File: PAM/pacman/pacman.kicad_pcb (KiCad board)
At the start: 2 copper layers, 92.7 x 66 mm, 20 parts, among them J1 Conn_01x08, J2 Conn_01x04, J6 TE Mate-N-Lok, J7 TE Mate-N-Lok, J8 TE Mate-N-Lok, J9 JST PH, K1 G2RL, K2 G5V-1, Q2 MMBT2222A

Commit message: working on layout
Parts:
- moved J7 77.4 mm to (72.9, 96.0), turned to 180 degrees
- moved R7 52.2 mm to (57.4, 124.2), turned to 90 degrees
- moved R4 51.0 mm to (47.5, 124.5), turned to 90 degrees
- moved F2 41.6 mm to (73.2, 119.4), turned to 90 degrees
- moved J8 38.1 mm to (86.7, 97.3)
- moved K1 31.5 mm to (40.3, 133.6)
- moved D1 30.8 mm to (87.6, 86.4), turned to 90 degrees
- moved D3 30.7 mm to (32.8, 133.3)
- moved R1 29.0 mm to (60.7, 79.0)
- moved F1 17.2 mm to (85.9, 125.2), turned to 90 degrees
- moved Q2 7.95 mm to (31.6, 112.8)
- moved R6 7.75 mm to (29.9, 107.2)
- moved R5 7.63 mm to (29.9, 109.2)
- moved J6 4.57 mm to (46.5, 80.4), turned to 90 degrees
- moved D5 0.76 mm to (14.7, 108.0), turned to -90 degrees
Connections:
- D3 pad 1: /TSV_SAFETY_LOOP -> /AIR_B-
- D5 pad 1: /TSV_SAFETY_LOOP -> /AIR_B-
- J1 pad 1: +12V -> GND
- J1 pad 2: /PRECHARGE -> GND
- J1 pad 3: /TSV_SAFETY_LOOP -> +12V
- J1 pad 4: /BMS_CAN+ -> /PRECHARGE
- J1 pad 5: /BMS_CAN- -> /BMS_CAN+
- J1 pad 6: /MAIN_CONT -> /AIR_B-
- J1 pad 7: unconnected-(J1-Pad7) -> /MAIN_CONT
- J1 pad 8: GND -> /BMS_CAN-
- J9 pad 1: /TSV_SAFETY_LOOP -> /AIR_B-
- K1 pad 2: /TSV_SAFETY_LOOP -> /AIR_B-
- K2 pad 10: /TSV_SAFETY_LOOP -> /AIR_B-
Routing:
- net /AIR_B-: track 0.00 -> 33.4 mm
- net /BMS_CAN+: track 0.00 -> 31.7 mm
- net /BMS_CAN-: track 0.00 -> 31.7 mm
- net +12V: track 0.00 -> 31.5 mm
- net /AIR_B+: track 0.00 -> 27.4 mm
- net /MAIN_CONT: track 0.00 -> 26.0 mm
- net /PRECHARGE: track 0.00 -> 22.3 mm
- net Net-(Q2-Pad1): track 0.00 -> 2.65 mm
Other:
- outline, holes or cut-outs redrawn

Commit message: DRC updating
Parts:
- removed J7, J8: TE Mate-N-Lok, AERO_Footprints:TE_MATE-N-LOK_1-770866-x_1x02_P4.14mm_Vertical
- added F3: Fuse, AERO_Footprints:Fuseholder_Blade_Mini_Keystone_3568, F.Cu at (185.0, 64.1)
- added G***: LOGO, AERO_Footprints:AERO_Logo_10x4mm, F.Cu at (181.1, 109.2)
- added High Voltage: Symbol_HighVoltage_Type2_CopperTop_VerySmall, Symbol:Symbol_HighVoltage_Type2_CopperTop_VerySmall, F.Cu at (129.8, 109.0)
- added J3: Conn_01x01, Connector_Hirose:Hirose_DF63M-1P-3.96DSA_1x01_P3.96mm_Vertical, F.Cu at (155.7, 111.0)
- added J4: Conn_01x01, Connector_Hirose:Hirose_DF63M-1P-3.96DSA_1x01_P3.96mm_Vertical, F.Cu at (129.3, 93.5)
- added J5: Conn_01x01, Connector_Hirose:Hirose_DF63M-1P-3.96DSA_1x01_P3.96mm_Vertical, F.Cu at (117.3, 106.9)
- added K3: G5V-1, Relay_THT:Relay_SPDT_Omron_G5V-1, F.Cu at (198.7, 63.4)
- D1: footprint LED_SMD:LED_0603_1608Metric_Pad1.05x0.95mm_HandSolder -> AERO_Footprints:LPA-C011301S-x LED 0805 LIGHT PIPE SINGLE VERT SMD
- D3, R1: moved to B.Cu
- J6: value TE Mate-N-Lok -> Conn_01x02; footprint AERO_Footprints:TE_MATE-N-LOK_1-770866-x_1x02_P4.14mm_Vertical -> Connector_JST:JST_XH_B2B-XH-A_1x02_P2.50mm_Vertical
- moved J2 193.6 mm to (195.6, 78.7), turned to 90 degrees
- moved J9 177.0 mm to (188.0, 78.0), turned to 90 degrees
- moved D5 174.8 mm to (187.8, 83.7), turned to 90 degrees
- moved K2 163.8 mm to (181.6, 79.9), turned to 180 degrees
- moved J1 163.3 mm to (182.9, 98.9), turned to 0 degrees
- moved D4 162.4 mm to (179.2, 73.0), turned to 180 degrees
- moved D3 156.4 mm to (172.1, 62.4), turned to 90 degrees
- moved R5 145.2 mm to (172.7, 82.4), turned to 0 degrees
- moved R6 144.5 mm to (172.7, 84.5), turned to 0 degrees
- moved Q2 143.5 mm to (171.0, 78.9), turned to 180 degrees
- moved K1 135.0 mm to (154.9, 62.4), turned to 180 degrees
- moved J6 133.7 mm to (178.1, 56.4), turned to -90 degrees
- moved R4 119.2 mm to (155.1, 73.0), turned to -90 degrees
- moved R7 101.5 mm to (145.2, 73.3), turned to -90 degrees
- moved R1 86.7 mm to (140.7, 112.3), turned to 90 degrees
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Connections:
- J1 pad 2: GND -> /BMS_FAN
- J6 pad 1: /INT+ -> Net-(F3-Pad2)
- J6 pad 2: /INT+ -> GND
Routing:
- net /INT-: track 0.00 -> 52.0 mm
- net /BMS_FAN: track 0.00 -> 47.7 mm
- net Net-(F1-Pad1): track 0.00 -> 40.8 mm
- net +12V: track 31.5 -> 70.3 mm
- net /INT+: track 0.00 -> 28.5 mm
- net Net-(D3-Pad2): track 0.00 -> 24.3 mm, vias 0 -> 1
- net /AIR_B-: track 33.4 -> 56.2 mm
- net Net-(K1-Pad5): track 0.00 -> 18.3 mm
- net Net-(F2-Pad1): track 0.00 -> 14.6 mm
- net Net-(D1-Pad2): track 0.00 -> 13.0 mm
- net Net-(F3-Pad2): track 0.00 -> 11.2 mm
- net /FAN_OUT: track 0.00 -> 8.82 mm
- net /B+: track 0.00 -> 7.26 mm
- net /BMS_CAN+: track 31.7 -> 28.7 mm
- net /BMS_CAN-: track 31.7 -> 28.7 mm
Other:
- outline, holes or cut-outs redrawn
- board text added: "BATT+"
- board text added: "G.Spearing 22.032"
- board text added: "GLV"
- board text added: "INT+"
- board text added: "INT-"
- board text added: "TSV"

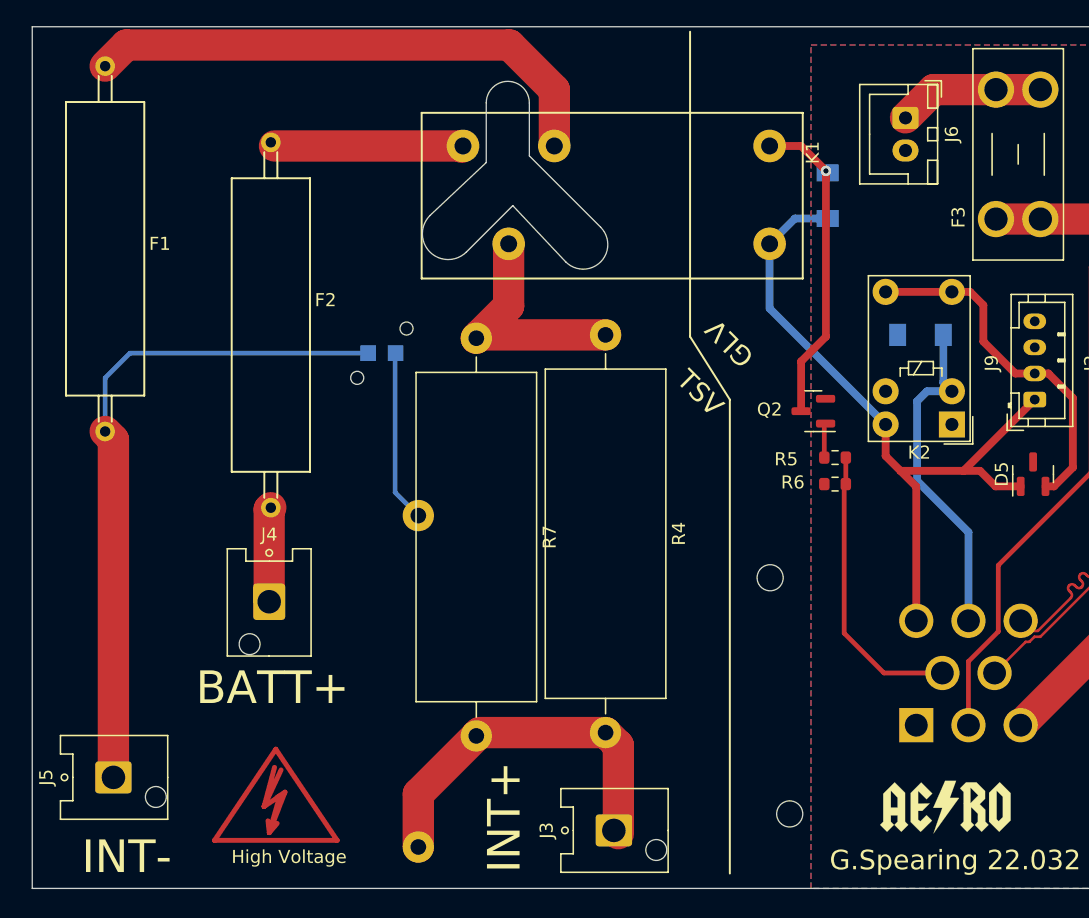
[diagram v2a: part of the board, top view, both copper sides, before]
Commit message: updating side 2 mirror
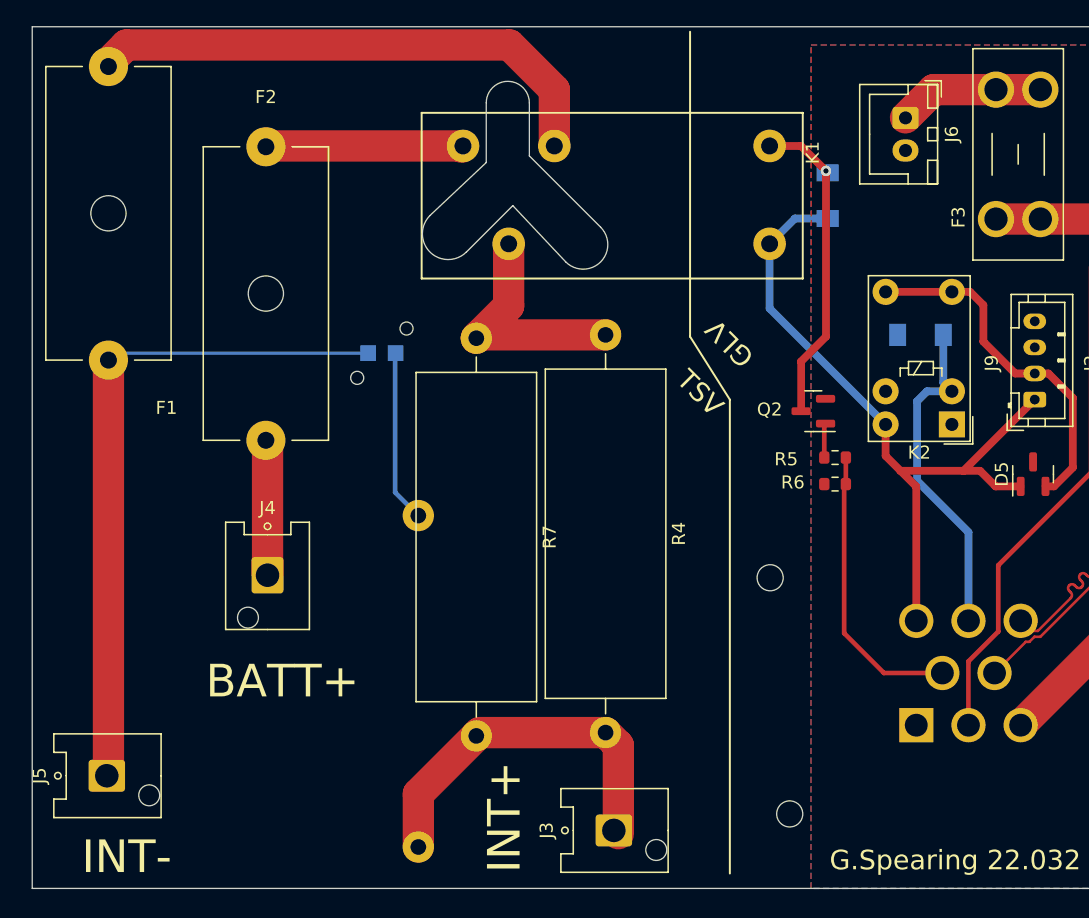
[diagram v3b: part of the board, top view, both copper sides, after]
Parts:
- removed G***: LOGO, AERO_Footprints:AERO_Logo_10x4mm
- removed High Voltage: Symbol_HighVoltage_Type2_CopperTop_VerySmall, Symbol:Symbol_HighVoltage_Type2_CopperTop_VerySmall
- F1, F2: footprint AERO_Footprints:Bell_0ADKP1000-RE -> AERO_Footprints:Fuseholder_Cylinder-5x20mm_Schurter_0031_8201_Horizontal_Open_3d
- moved F1 14.0 mm to (117.0, 52.5)
- moved F2 13.7 mm to (129.0, 58.6)
- moved J4 2.04 mm to (129.2, 91.4)
- moved J5 0.52 mm to (116.8, 106.8)
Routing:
- net /B+: track 7.26 -> 10.4 mm

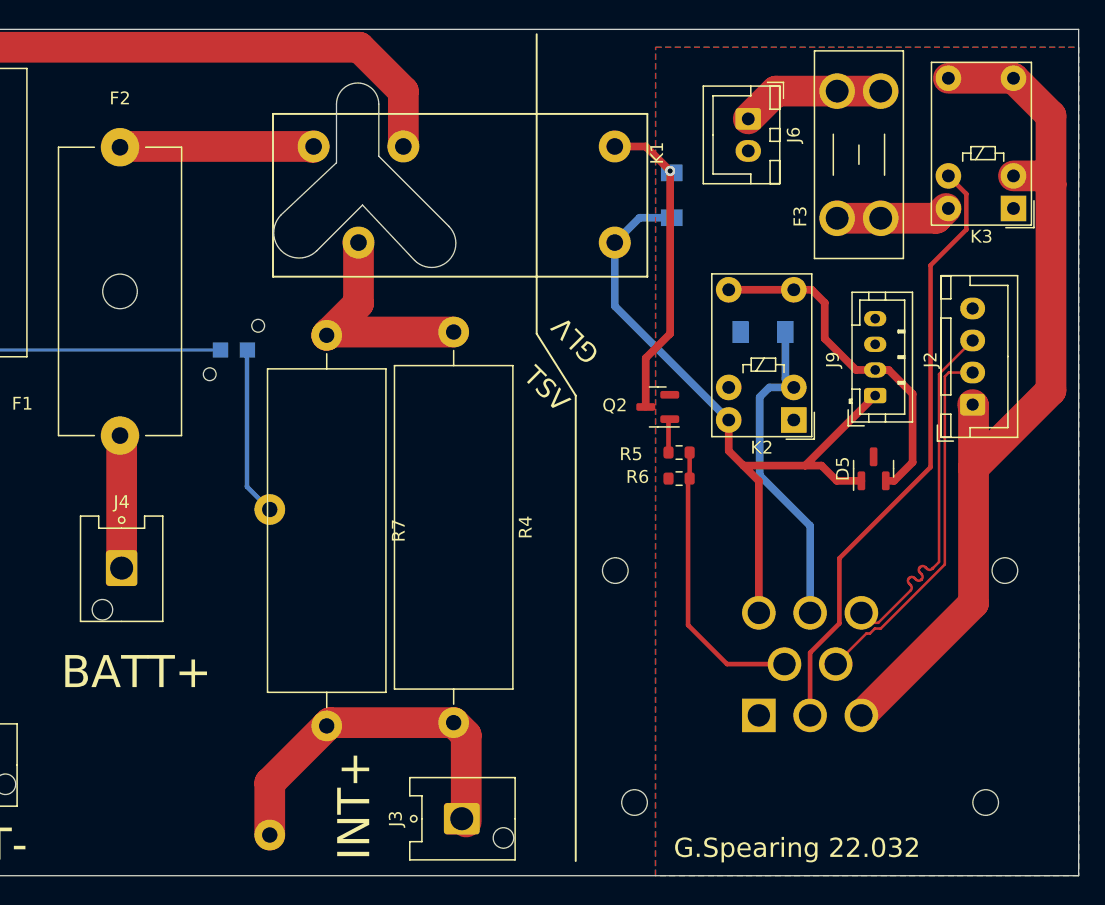
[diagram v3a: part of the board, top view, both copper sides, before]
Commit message: layout and labeling update
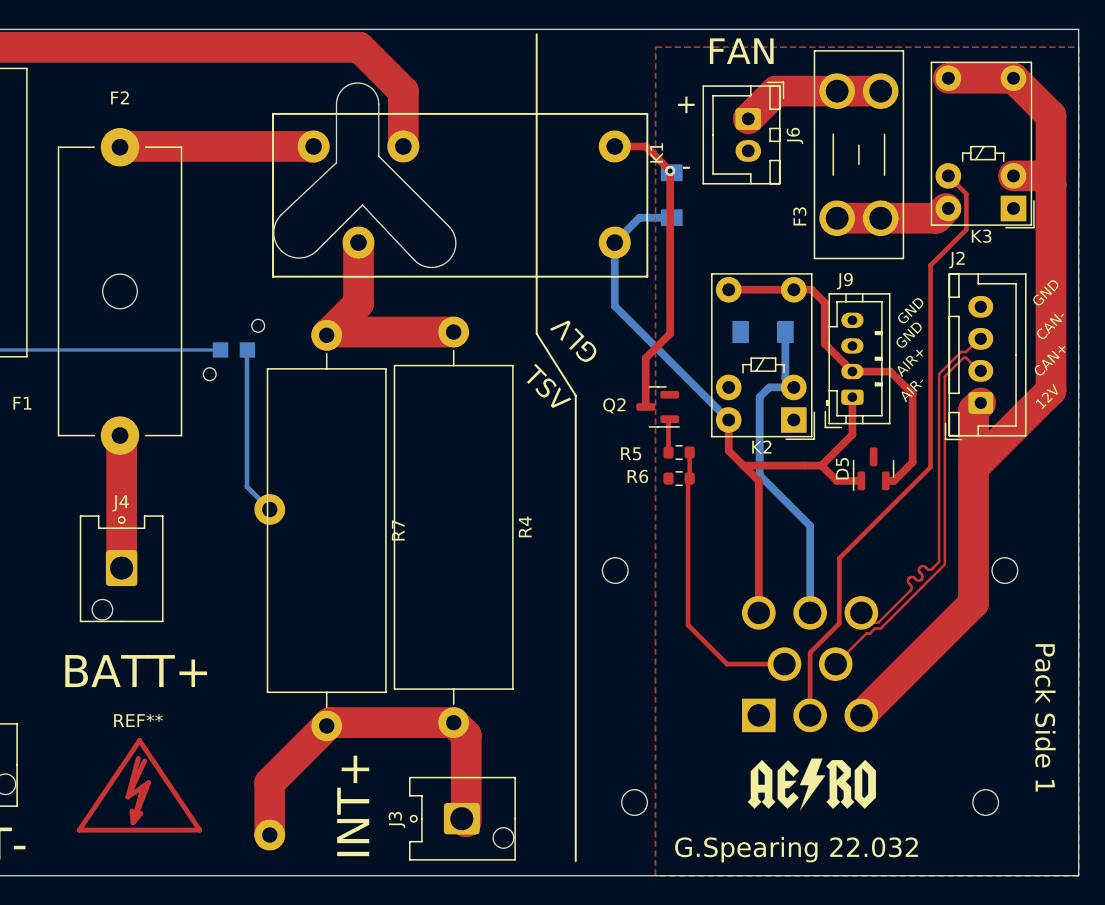
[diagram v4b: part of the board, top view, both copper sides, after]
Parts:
- added G***: LOGO, AERO_Footprints:AERO_Logo_10x4mm, F.Cu at (183.0, 108.3)
- added REF**: Symbol_HighVoltage_Type2_CopperTop_VerySmall, Symbol:Symbol_HighVoltage_Type2_CopperTop_VerySmall, F.Cu at (130.6, 109.1)
- moved J9 1.78 mm to (186.2, 78.1)
- moved J2 0.65 mm to (196.2, 78.6)
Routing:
- net /BMS_CAN+: track 28.7 -> 30.2 mm
- net /AIR_B-: track 56.2 -> 54.8 mm
- net /BMS_CAN-: track 28.7 -> 29.4 mm
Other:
- board text added: "+ -"
- board text added: "12V"
- board text added: "AIR+"
- board text added: "AIR-"
- board text added: "CAN+"
- board text added: "CAN-"
- board text added: "FAN"
- board text added: "GND"
- board text added: "Pack Side 1"

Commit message: Adding CAN termination resistors
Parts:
- removed G***: LOGO, AERO_Footprints:AERO_Logo_10x4mm
- removed REF**: Symbol_HighVoltage_Type2_CopperTop_VerySmall, Symbol:Symbol_HighVoltage_Type2_CopperTop_VerySmall
- added R2: 120, Resistor_SMD:R_0603_1608Metric_Pad0.98x0.95mm_HandSolder, F.Cu at (192.2, 89.8)
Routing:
- net /BMS_CAN-: track 29.4 -> 32.2 mm
- net /BMS_CAN+: track 30.2 -> 31.2 mm

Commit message: updating silkscreen objects
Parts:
- moved F1 0.11 mm to (116.9, 52.4)

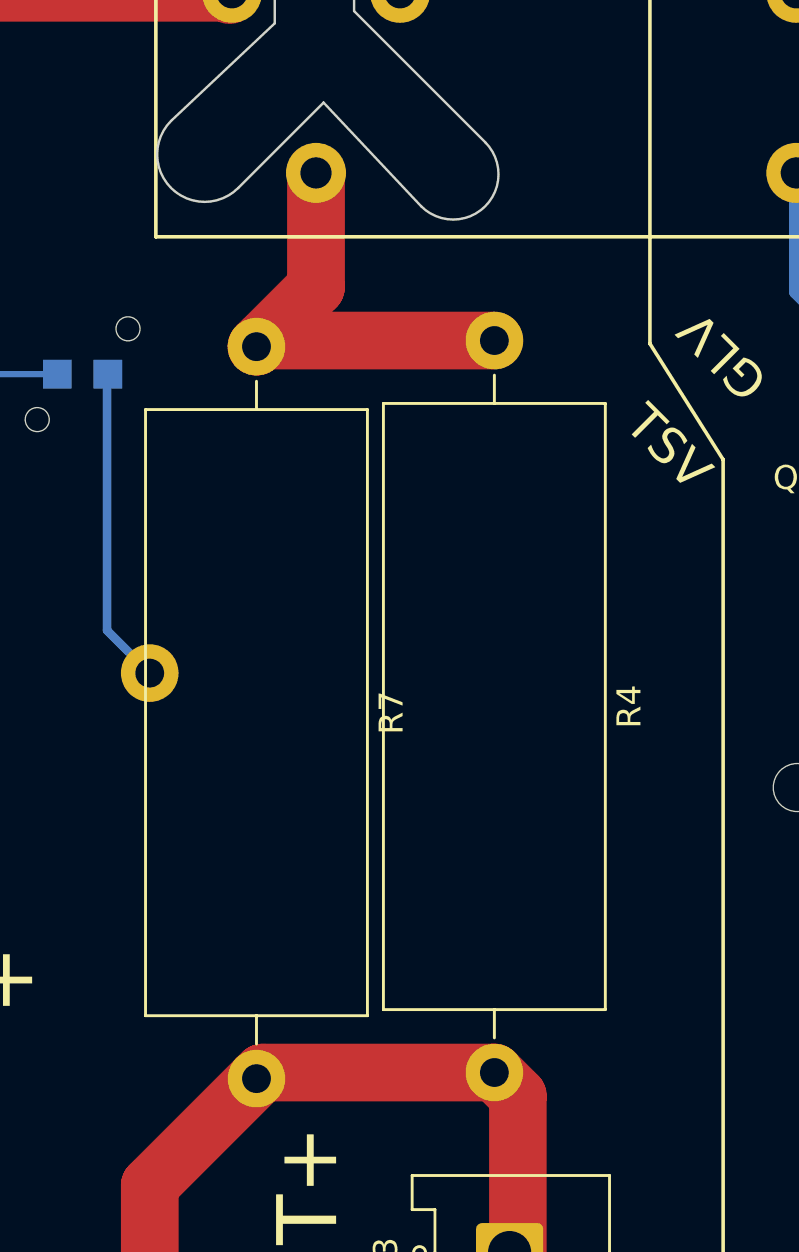
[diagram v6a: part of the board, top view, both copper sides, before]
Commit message: Major Review and Part Update
updating footprints, component values, layouts
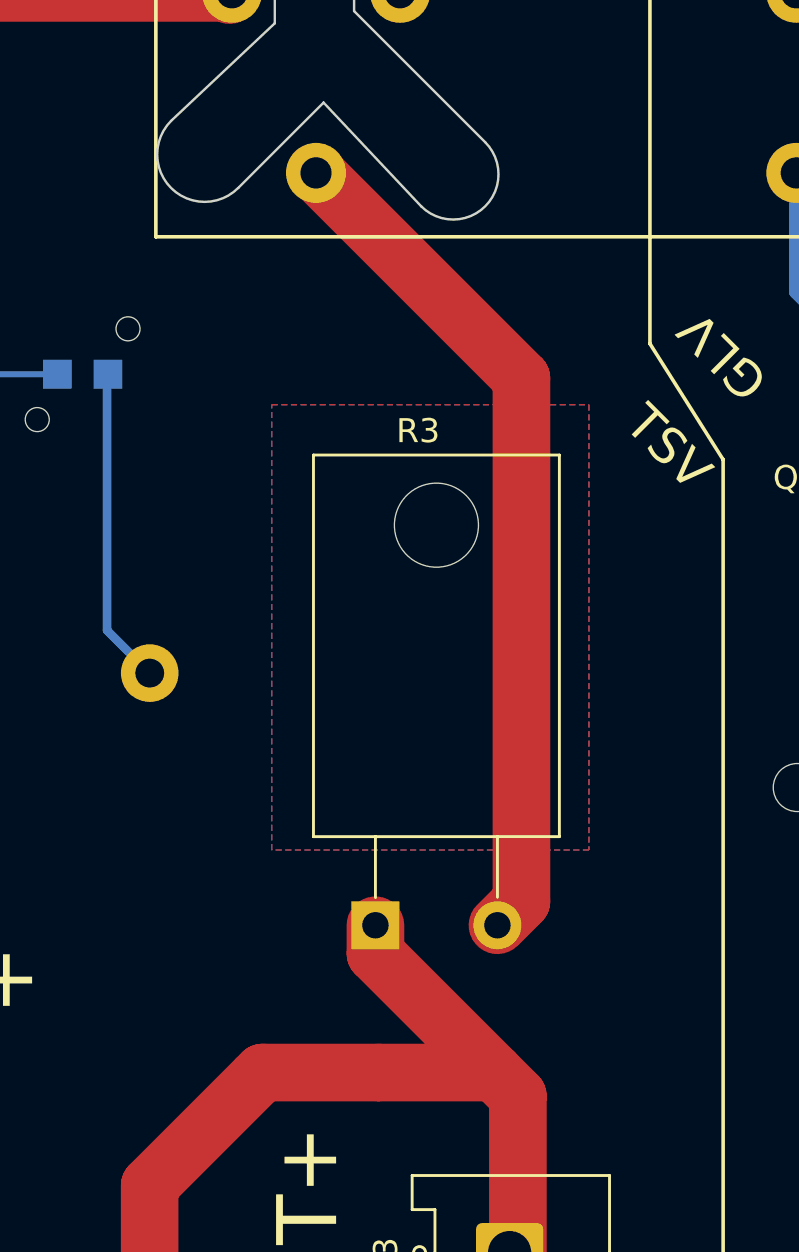
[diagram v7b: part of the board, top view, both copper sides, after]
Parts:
- removed R4, R7: 1k 7W, Resistor_THT:R_Axial_Power_L25.0mm_W9.0mm_P30.48mm
- added R3: 500, Package_TO_SOT_THT:TO-220-2_Horizontal_TabDown, F.Cu at (150.1, 97.4)
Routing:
- net Net-(K1-Pad5): track 18.3 -> 35.3 mm
- net /INT+: track 28.5 -> 36.7 mm
- added copper zone on B.Cu, net (none)
- added copper zone on F.Cu, net (none)
